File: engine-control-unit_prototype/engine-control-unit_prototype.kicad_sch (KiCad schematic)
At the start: 329 parts, among them IC1 TPS259573DSGR, J1 JTAG, J10 PORT_B, J11 PORT_C, J12 PORT_D, J13 PORT_A, J14 PORT_G, J15 PORT_F, J16 PORT_E, J17 2S_18650, J18 VALVE_IPA, J19 VALVE_NOS, J2 USB_C_Receptacle_USB2.0_man, J20 HEATER_IPA, J21 HEATER_NOS, J22 THERM2, J23 MAG_CONN_1, J24 MAG_CONN_2, J25 I2C_A, J26 THERM1, J27 I2C_B, J28 I2C_C, J29 I2C_D, J3 Micro_SD_Card_Det1, J4 PT1, J5 VREF, J6 PT1, J7 VREF, J8 FDCAN, J9 ADXL345, Q1 PMOS, Q2 NMOS, Q3 NPN, Q4 NMOS, Q5 NPN, Q6 NPN, SW1 BOOT, U1 USBLC6-2SC6, U10 TPS55285, U13 INA219AxD, U14 LT3042xMSE, U3 INA826, U4 INA826, U5 TCAN337G, U6 INA219AxD, U7 STM32H747II, U8 INA219AxD, U9 TPS55285, Y1 32.768KHz, Y2 25MHz

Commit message: Some fixes Back to subsheets Missing new ADC boost ldo for 3V3 now
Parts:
- removed C30: 0.1uF, Capacitor_SMD:C_0603_1608Metric_Pad1.08x0.95mm_HandSolder, symbol 0CSL_D1_V1:CAP_7mm_X_2mm
- removed C31: 10uF/50V, symbol Device:C_Polarized_US
- removed C32, C44, C53, C55, C57, C62, C63, C64, C65, C66, C75, C76, C77, C78, C79, C80, C81, C82, C83, C84, C85: C, symbol Device:C
- removed C33, C35, C40, C48, C49, C50, C52, C54, C56, C61, C86, C87, C88, C92: 0.1u, symbol Device:C
- removed C34, C41, C51: 10u, symbol Device:C
- removed C36, C37, C39, C42, C43, C45: ?, symbol Device:C
- removed C38: DNF, symbol Device:C
- removed C46: 100nF, symbol Device:C
- removed C47: 2.2u, symbol Device:C
- removed C58: CIN, symbol Device:C_Polarized_US
- removed C59: COUT, symbol Device:C_Polarized_US
- removed C60: CdV/dT, symbol Device:C
- removed C90, C91: 1uF, Capacitor_SMD:C_0603_1608Metric_Pad1.08x0.95mm_HandSolder, symbol Device:C
- removed D2: 6.4V, Diode_SMD:D_0603_1608Metric_Pad1.05x0.95mm_HandSolder, symbol 0CSL_D1_V1:DIODE_SCHOTTKY_30V_200mA
- removed D3: TVS SMBJ, symbol Device:D_Schottky
- removed D6: D_Zener, symbol Device:D_Zener
- removed F1: Polyfuse, Fuse:Fuse_0603_1608Metric_Pad1.05x0.95mm_HandSolder, symbol Device:Polyfuse_Small
- removed IC1: TPS259573DSGR, SON50P200X200X80-9N, symbol TPS259573DSGR:TPS259573DSGR
- removed J1: JTAG, UserFootprints:490107670612, symbol Connector_Generic:Conn_02x03_Counter_Clockwise
- removed J17: 2S_18650, symbol Connector:Screw_Terminal_01x02
- removed J2: USB_C_Receptacle_USB2.0_man, Connector_USB:USB_C_Receptacle_GCT_USB4105-xx-A_16P_TopMnt_Horizontal, symbol 0CSL_D1_V1:USB_C_Receptacle_USB2.0_man
- removed J22: THERM2, UserFootprints:MOLEX_5013310207, symbol Connector_Generic_MountingPin:Conn_01x02_MountingPin
- removed J25: I2C_A, symbol Connector:Conn_01x04_Socket
- removed J26: THERM1, UserFootprints:MOLEX_5013310207, symbol Connector_Generic_MountingPin:Conn_01x02_MountingPin
- removed J27: I2C_B, symbol Connector:Conn_01x04_Socket
- removed J28: I2C_C, symbol Connector:Conn_01x04_Socket
- removed J29: I2C_D, symbol Connector:Conn_01x04_Socket
- removed J3: Micro_SD_Card_Det1, UserFootprints:GCT_MEM2075-00-140-01-A, symbol Connector:Micro_SD_Card_Det1
- removed J4, J6: PT1, symbol Connector:Screw_Terminal_01x04
- removed J5, J7: VREF, symbol Connector:Conn_01x01_Pin
- removed J8: FDCAN, symbol Connector:DE9_Pins_MountingHoles
- removed J9: ADXL345, symbol Connector:Conn_01x09_Socket
- removed JP3, JP4: PIN/GND, symbol Jumper:Jumper_3_Bridged12
- removed L1, L2: L, symbol Device:L
- removed Q1: PMOS, symbol Simulation_SPICE:PMOS
- removed R1, R100, R101, R102, R11, R12, R140, R5, R7, R77, R78, R8, R9, R97, R98, R99: 0, symbol Device:R_US
- removed R10, R6, R67: ?, symbol Device:R_US
- removed R13, R22, R23, R25, R26, R27, R28, R30, R31, R37, R40, R55, R56, R57, R58, R59, R61, R63, R64, R70, R83, R84, R85, R86, R87, R88, R89, R90, R91, R92, R93, R94: R_US, symbol Device:R_US
- removed R14, R15, R16, R17, R18, R19, R20, R21, R24, R32, R33, R49, R50, R51, R52, R53, R54: 10k, symbol Device:R_US
- removed R29, R41: 10m, symbol Device:R_US
- removed R3, R4: 5.1k, symbol Device:R_US
- removed R60: 200k, symbol Device:R_US
- removed R62: DNF, symbol Device:R_US
- removed R68, R69: 10k, Resistor_SMD:R_0603_1608Metric_Pad0.98x0.95mm_HandSolder, symbol Device:R
- removed R81, R82: 60, symbol Device:R_US
- removed TP1: PT1, symbol Connector:TestPoint
- removed TP10: IN2-, symbol Connector:TestPoint
- removed TP11: IN3+, symbol Connector:TestPoint
- removed TP12: IN3-, symbol Connector:TestPoint
- removed TP13: VDD_3V3, symbol Connector:TestPoint
- removed TP14: CANH, symbol Connector:TestPoint
- removed TP15: CANL, symbol Connector:TestPoint
- removed TP16: TH1, symbol Connector:TestPoint
- removed TP17: TH2, symbol Connector:TestPoint
- removed TP2: PT2, symbol Connector:TestPoint
- removed TP3: VDD_10V, symbol Connector:TestPoint
- removed TP4: TPS10V_OUT, symbol Connector:TestPoint
- removed TP5: BATT1, symbol Connector:TestPoint
- removed TP6: VBATT_SAFE, symbol Connector:TestPoint
- removed TP7: IN1+, symbol Connector:TestPoint
- removed TP8: IN1-, symbol Connector:TestPoint
- removed TP9: IN2+, symbol Connector:TestPoint
- removed U1: USBLC6-2SC6, Package_TO_SOT_SMD:SOT-23-6, symbol Power_Protection:USBLC6-2SC6
- removed U10, U9: TPS55285, symbol SiriusLib:TPS55285
- removed U13, U6, U8: INA219AxD, Package_SO:SOIC-8_3.9x4.9mm_P1.27mm, symbol Sensor_Energy:INA219AxD
- removed U14: LT3042xMSE, Package_SO:MSOP-10-1EP_3x3mm_P0.5mm_EP1.68x1.88mm, symbol Regulator_Linear:LT3042xMSE
- removed U2: ~, Package_BGA:LFBGA-153_11.5x13mm_Layout14x14_P0.5mm, symbol FSU_LIB:ASFC32G31T3-51BIN
- removed U3, U4: INA826, UserFootprints:SOP65P490X110-8N, symbol INA826:INA826AIDGKR
- removed U5: TCAN337G, symbol Interface_CAN_LIN:TCAN337G
- added R144, R150, R153, R154: R_US, symbol Device:R_US
- added R151, R152, R157, R158, R159, R160, R161, R162, R163, R164, R165, R166, R167, R168, R169, R170, R171, R172, R173, R174, R175, R176, R177, R178, R179, R180, R181, R182, R183, R184, R185, R186, R187, R188, R189, R190, R191, R192, R193, R194, R195, R196, R197, R198, R199, R200, R201, R202, R203, R204, R205, R206, R207, R208, R209, R210, R211, R212, R213, R214, R215, R216, R217, R218, R219, R220, R221, R222, R223, R224, R225, R226, R227: 0, symbol Device:R_US
- R42: value 10m -> 0
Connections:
- net ADXL_CS is gone; now on an unnamed net: R114.2
- net ADXL_SCL is gone; now on an unnamed net: R111.2
- net ADXL_SDA is gone; now on an unnamed net: R112.2
- net D+ is gone; now on an unnamed net: R136.2
- net I2CD_SDA is gone; now on an unnamed net: R107.2
- net Psense2_IN+ is gone; now on net VDD_3V3: R42.1
- net SD_CLK is gone; now on an unnamed net: R79.2
- net SD_CMD is gone; now on an unnamed net: R80.2
- net SD_DAT0 is gone; now on an unnamed net: R95.2
- net SD_DAT1 is gone; now on an unnamed net: R96.2
- net THERM1 is gone; now on an unnamed net: R109.2
- net TPS10V_SCL is gone; now on an unnamed net: R106.2
- net TPS3V3_SCL is gone; now on an unnamed net: R104.2
- net DATA_S1: no longer R122.2
- net DATA_S2: no longer R123.2
- net GND: now also R150.1, R153.1, R154.1; no longer Q3.3 (E), Q5.3 (E), Q6.3 (E)
- net LSE0: no longer R129.2
- net LSE1: no longer R130.2
- net NRST: now also R144.2; no longer R125.2
- net VDD_3V3: no longer R42.2
- net VDD_MCU: now also R144.1
- net at J15.1 (Pin_1): now also R115.1; no longer U7.18 (PF0)
- net at J15.10 (Pin_10): now also R124.1; no longer U7.29 (PF9)
- net at J15.11 (Pin_11): now also R125.1; no longer U7.30 (PF10)
- net at J15.12 (Pin_12): now also R126.1; no longer U7.58 (PF11)
- net at J15.13 (Pin_13): now also R127.1; no longer U7.59 (PF12)
- net at J15.14 (Pin_14): now also R128.1; no longer U7.60 (PF13)
- net at J15.15 (Pin_15): now also R129.1; no longer U7.61 (PF14)
- net at J15.16 (Pin_16): now also R130.1; no longer U7.62 (PF15)
- net at J15.2 (Pin_2): now also R116.1; no longer U7.19 (PF1)
- net at J15.3 (Pin_3): now also R117.1; no longer U7.20 (PF2)
- net at J15.4 (Pin_4): now also R118.1; no longer U7.21 (PF3)
- net at J15.5 (Pin_5): now also R119.1; no longer U7.22 (PF4)
- net at J15.6 (Pin_6): now also R120.1; no longer U7.23 (PF5)
- net at J15.7 (Pin_7): now also R121.1; no longer U7.26 (PF6)
- net at J15.8 (Pin_8): now also R122.1; no longer U7.27 (PF7)
- net at J15.9 (Pin_9): now also R123.1; no longer U7.28 (PF8)
- net at R136.1: now also J10.3 (Pin_3)
- net at J16.1 (Pin_1): now also R196.2; no longer U7.170 (PE0)
- net at J16.10 (Pin_10): now also R205.2; no longer U7.69 (PE9)
- net at J16.11 (Pin_11): now also R206.2; no longer U7.72 (PE10)
- net at J16.12 (Pin_12): now also R207.2; no longer U7.73 (PE11)
- net at U7.74 (PE12): now also R208.1; no longer J16.13 (Pin_13)
- net at J16.14 (Pin_14): now also R209.2; no longer U7.75 (PE13)
- net at J16.15 (Pin_15): now also R210.2; no longer U7.76 (PE14)
- net at J16.16 (Pin_16): now also R211.2; no longer U7.77 (PE15)
- net at J16.2 (Pin_2): now also R197.2; no longer U7.171 (PE1)
- net at J16.3 (Pin_3): now also R198.2; no longer U7.1 (PE2)
- net at J16.4 (Pin_4): now also R199.2; no longer U7.2 (PE3)
- net at J16.5 (Pin_5): now also R200.2; no longer U7.3 (PE4)
- net at U7.4 (PE5): now also R201.1; no longer J16.6 (Pin_6)
- net at J16.7 (Pin_7): now also R202.2; no longer U7.5 (PE6)
- net at J16.8 (Pin_8): now also R203.2; no longer U7.67 (PE7)
- net at J16.9 (Pin_9): now also R204.2; no longer U7.68 (PE8)
- net at R107.1: now also J14.9 (Pin_9)
- net at R95.1: now also J14.3 (Pin_3)
- net at J10.1 (Pin_1): now also R133.1; no longer U7.55 (PB0)
- net at J10.10 (Pin_10): now also R157.1; no longer U7.169 (PB9)
- net at J10.11 (Pin_11): now also R158.1; no longer U7.78 (PB10)
- net at J10.12 (Pin_12): now also R159.1; no longer U7.79 (PB11)
- net at J10.13 (Pin_13): now also R160.1; no longer U7.85 (PB12)
- net at J10.14 (Pin_14): now also R161.1; no longer U7.86 (PB13)
- net at J10.15 (Pin_15): now also R162.1; no longer U7.87 (PB14)
- net at J10.16 (Pin_16): now also R163.1; no longer U7.88 (PB15)
- net at J10.2 (Pin_2): now also R134.1; no longer U7.56 (PB1)
- net at U7.57 (PB2): no longer J10.3 (Pin_3)
- net at J10.4 (Pin_4): now also R137.1; no longer U7.162 (PB3)
- net at J10.5 (Pin_5): now also R141.1; no longer U7.163 (PB4)
- net at J10.6 (Pin_6): now also R142.1; no longer U7.164 (PB5)
- net at J10.7 (Pin_7): now also R143.1; no longer U7.165 (PB6)
- net at J10.8 (Pin_8): now also R151.1; no longer U7.166 (PB7)
- net at J10.9 (Pin_9): now also R152.1; no longer U7.168 (PB8)
- net at J13.1 (Pin_1): now also R212.2; no longer U7.41 (PA0)
- net at J13.10 (Pin_10): now also R221.2; no longer U7.128 (PA9)
- net at J13.11 (Pin_11): now also R222.2; no longer U7.129 (PA10)
- net at U7.130 (PA11): now also R223.1; no longer J13.12 (Pin_12)
- net at J13.13 (Pin_13): now also R224.2; no longer U7.131 (PA12)
- net at J13.14 (Pin_14): now also R225.2; no longer U7.132 (PA13)
- net at U7.138 (PA14): now also R226.1; no longer J13.15 (Pin_15)
- net at J13.16 (Pin_16): now also R227.2; no longer U7.139 (PA15)
- net at U7.42 (PA1): now also R213.1; no longer J13.2 (Pin_2)
- net at J13.3 (Pin_3): now also R214.2; no longer U7.43 (PA2)
- net at J13.4 (Pin_4): now also R215.2; no longer U7.46 (PA3)
- net at J13.5 (Pin_5): now also R216.2; no longer U7.49 (PA4)
- net at J13.6 (Pin_6): now also R217.2; no longer U7.50 (PA5)
- net at J13.7 (Pin_7): now also R218.2; no longer U7.51 (PA6)
- net at J13.8 (Pin_8): now also R219.2; no longer U7.52 (PA7)
- net at J13.9 (Pin_9): now also R220.2; no longer U7.127 (PA8)
- net at U7.143 (PD0): now also R180.1; no longer J12.1 (Pin_1)
- net at J12.10 (Pin_10): now also R189.2; no longer U7.90 (PD9)
- net at J12.11 (Pin_11): now also R190.2; no longer U7.91 (PD10)
- net at J12.12 (Pin_12): now also R191.2; no longer U7.94 (PD11)
- net at U7.95 (PD12): now also R192.1; no longer J12.13 (Pin_13)
- net at J12.14 (Pin_14): now also R193.2; no longer U7.96 (PD13)
- net at J12.15 (Pin_15): now also R194.2; no longer U7.97 (PD14)
- net at J12.16 (Pin_16): now also R195.2; no longer U7.98 (PD15)
- net at J12.2 (Pin_2): now also R181.2; no longer U7.144 (PD1)
- net at J12.3 (Pin_3): now also R182.2; no longer U7.145 (PD2)
- net at J12.4 (Pin_4): now also R183.2; no longer U7.146 (PD3)
- net at J12.5 (Pin_5): now also R184.2; no longer U7.147 (PD4)
- net at J12.6 (Pin_6): now also R185.2; no longer U7.148 (PD5)
- net at J12.7 (Pin_7): now also R186.2; no longer U7.149 (PD6)
- net at U7.150 (PD7): now also R187.1; no longer J12.8 (Pin_8)
- net at J12.9 (Pin_9): now also R188.2; no longer U7.89 (PD8)
- net at R104.1: now also J14.6 (Pin_6)
- net at R96.1: now also J14.4 (Pin_4)
- net at U7.10 (PC14): now also R178.2; no longer J11.15 (Pin_15)
- net at U7.11 (PC15): now also R179.2; no longer J11.16 (Pin_16)
- net at J11.7 (Pin_7): now also R170.1; no longer U7.122 (PC6)
- net at J11.8 (Pin_8): now also R171.1; no longer U7.123 (PC7)
- net at U7.124 (PC8): now also R172.2; no longer J11.9 (Pin_9)
- net at J11.10 (Pin_10): now also R173.1; no longer U7.125 (PC9)
- net at J11.11 (Pin_11): now also R174.1; no longer U7.140 (PC10)
- net at U7.141 (PC11): now also R175.2; no longer J11.12 (Pin_12)
- net at J11.13 (Pin_13): now also R176.1; no longer U7.142 (PC12)
- net at U7.34 (PC0): now also R164.2; no longer J11.1 (Pin_1)
- net at U7.35 (PC1): now also R165.2; no longer J11.2 (Pin_2)
- net at U7.36 (PC2_C): now also R166.2; no longer J11.3 (Pin_3)
- net at U7.37 (PC3_C): now also R167.2; no longer J11.4 (Pin_4)
- net at U7.53 (PC4): now also R168.2; no longer J11.5 (Pin_5)
- net at J11.6 (Pin_6): now also R169.1; no longer U7.54 (PC5)
- net at J11.14 (Pin_14): now also R177.1; no longer U7.9 (PC13)
- net at R114.1: now also J14.16 (Pin_16)
- net at R79.1: now also J14.1 (Pin_1)
- net at R106.1: now also J14.8 (Pin_8)
- net at U7.110 (PG2): no longer J14.3 (Pin_3)
- net at U7.111 (PG3): no longer J14.4 (Pin_4)
- net at J14.5 (Pin_5): now also R103.1; no longer U7.114 (PG4)
- net at U7.115 (PG5): no longer J14.6 (Pin_6)
- net at J14.7 (Pin_7): now also R105.1; no longer U7.116 (PG6)
- net at U7.117 (PG7): no longer J14.8 (Pin_8)
- net at U7.118 (PG8): no longer J14.9 (Pin_9)
- net at J14.10 (Pin_10): now also R108.1; no longer U7.153 (PG9)
- net at U7.154 (PG10): no longer J14.11 (Pin_11)
- net at J14.12 (Pin_12): now also R110.1; no longer U7.155 (PG11)
- net at U7.156 (PG12): no longer J14.13 (Pin_13)
- net at U7.157 (PG13): no longer J14.14 (Pin_14)
- net at J14.15 (Pin_15): now also R113.1; no longer U7.158 (PG14)
- net at U7.161 (PG15): no longer J14.16 (Pin_16)
- net at U7.63 (PG0): no longer J14.1 (Pin_1)
- net at U7.66 (PG1): no longer J14.2 (Pin_2)
- net at R80.1: now also J14.2 (Pin_2)
- net at R111.1: now also J14.13 (Pin_13)
- net at R112.1: now also J14.14 (Pin_14)
- net at R109.1: now also J14.11 (Pin_11)
- net ADXL_SDO: no longer names the net of R113.2
- net ADXL_SDO: now also U7.158 (PG14)
- net BUZ: no longer names the net of R124.2
- net BUZ: now also U7.29 (PF9)
- net D-: no longer names the net of R137.2
- net D-: now also U7.162 (PB3)
- net EFUSE_FLT: no longer names the net of R141.2
- net EFUSE_FLT: now also U7.163 (PB4)
- net I2CD_SCL: no longer names the net of R108.2
- net I2CD_SCL: now also U7.153 (PG9)
- net PT1: no longer names the net of R133.2
- net PT1: now also U7.55 (PB0)
- net PT2: no longer names the net of R134.2
- net PT2: now also U7.56 (PB1)
- net SD_DAT2: no longer names the net of R115.2
- net SD_DAT2: now also U7.18 (PF0)
- net SD_DAT3: no longer names the net of R116.2
- net SD_DAT3: now also U7.19 (PF1)
- net SD_DET: no longer names the net of R117.2
- net SD_DET: now also U7.20 (PF2)
- net SWCLK: no longer names the net of R127.2
- net SWCLK: now also U7.59 (PF12)
- net SWDIO: no longer names the net of R126.2
- net SWDIO: now also U7.58 (PF11)
- net SWO: no longer names the net of R128.2
- net SWO: now also U7.60 (PF13)
- net TCAN_FLT: no longer names the net of R120.2
- net TCAN_FLT: now also U7.23 (PF5)
- net TCAN_RX: no longer names the net of R118.2
- net TCAN_RX: now also U7.21 (PF3)
- net TCAN_STBY: no longer names the net of R121.2
- net TCAN_STBY: now also U7.26 (PF6)
- net TCAN_TX: no longer names the net of R119.2
- net TCAN_TX: now also U7.22 (PF4)
- net THERM2: no longer names the net of R110.2
- net THERM2: now also U7.155 (PG11)
- net TPS10V_INT: no longer names the net of R142.2
- net TPS10V_INT: now also U7.164 (PB5)
- net TPS10V_SDA: no longer names the net of R105.2
- net TPS10V_SDA: now also U7.116 (PG6)
- net TPS3V3_INT: no longer names the net of R143.2
- net TPS3V3_INT: now also U7.165 (PB6)
- net TPS3V3_SDA: no longer names the net of R103.2
- net TPS3V3_SDA: now also U7.114 (PG4)
- net VDDA renamed VDDA_MCU
- net VDDA_MCU: now also R42.2
- new net: J16.13 (Pin_13), R208.2
- new net: R177.2, U7.9 (PC13)
- new net: J16.6 (Pin_6), R201.2
- new net: R171.2, U7.123 (PC7)
- new net: J13.15 (Pin_15), R226.2
- new net: R176.2, U7.142 (PC12)
- new net: Q5.3 (E), R153.2
- new net: J13.12 (Pin_12), R223.2
- new net: R122.2, U7.27 (PF7)
- new net: J13.2 (Pin_2), R213.2
- new net: Q6.3 (E), R150.2
- new net: R158.2, U7.78 (PB10)
- new net: J12.13 (Pin_13), R192.2
- new net: R125.2, U7.30 (PF10)
- new net: R173.2, U7.125 (PC9)
- new net: R216.1, U7.49 (PA4)
- new net: J12.1 (Pin_1), R180.2
- new net: R217.1, U7.50 (PA5)
- new net: R159.2, U7.79 (PB11)
- new net: J12.8 (Pin_8), R187.2
- new net: Q3.3 (E), R154.2
- new net: R162.2, U7.87 (PB14)
- new net: R174.2, U7.140 (PC10)
- new net: R207.1, U7.73 (PE11)
- new net: R169.2, U7.54 (PC5)
- new net: R202.1, U7.5 (PE6)
- new net: R170.2, U7.122 (PC6)
- new net: R186.1, U7.149 (PD6)
- new net: R189.1, U7.90 (PD9)
- new net: R218.1, U7.51 (PA6)
- new net: R161.2, U7.86 (PB13)
- new net: R181.1, U7.144 (PD1)
- new net: R185.1, U7.148 (PD5)
- new net: R194.1, U7.97 (PD14)
- new net: R209.1, U7.75 (PE13)
- new net: R204.1, U7.68 (PE8)
- new net: R129.2, U7.61 (PF14)
- new net: R182.1, U7.145 (PD2)
- new net: R183.1, U7.146 (PD3)
- new net: R184.1, U7.147 (PD4)
- new net: R151.2, U7.166 (PB7)
- new net: R152.2, U7.168 (PB8)
- new net: R157.2, U7.169 (PB9)
- new net: R160.2, U7.85 (PB12)
- new net: R163.2, U7.88 (PB15)
- new net: R188.1, U7.89 (PD8)
- new net: R190.1, U7.91 (PD10)
- new net: R191.1, U7.94 (PD11)
- new net: R193.1, U7.96 (PD13)
- new net: R195.1, U7.98 (PD15)
- new net: R224.1, U7.131 (PA12)
- new net: R206.1, U7.72 (PE10)
- new net: R220.1, U7.127 (PA8)
- new net: R203.1, U7.67 (PE7)
- new net: J11.16 (Pin_16), R179.1
- new net: R214.1, U7.43 (PA2)
- new net: R212.1, U7.41 (PA0)
- new net: J11.9 (Pin_9), R172.1
- new net: R227.1, U7.139 (PA15)
- new net: R219.1, U7.52 (PA7)
- new net: R198.1, U7.1 (PE2)
- new net: R221.1, U7.128 (PA9)
- new net: R222.1, U7.129 (PA10)
- new net: R225.1, U7.132 (PA13)
- new net: R196.1, U7.170 (PE0)
- new net: R197.1, U7.171 (PE1)
- new net: R199.1, U7.2 (PE3)
- new net: R123.2, U7.28 (PF8)
- new net: R200.1, U7.3 (PE4)
- new net: R215.1, U7.46 (PA3)
- new net: R130.2, U7.62 (PF15)
- new net: R205.1, U7.69 (PE9)
- new net: R210.1, U7.76 (PE14)
- new net: R211.1, U7.77 (PE15)
- new net: J11.2 (Pin_2), R165.1
- new net: J11.15 (Pin_15), R178.1
- new net: J11.4 (Pin_4), R167.1
- new net: J11.3 (Pin_3), R166.1
- new net: J11.1 (Pin_1), R164.1
- new net: J11.12 (Pin_12), R175.1
- new net: J11.5 (Pin_5), R168.1
- no-connect marks 21 -> 11
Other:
- added sheet ADC (adc.kicad_sch)
- added sheet COMMUNICATION (communication.kicad_sch)
- added sheet POWER (power.kicad_sch)
- added sheet STORAGE (storage.kicad_sch)
- note removed: "(1) This resistor is optional if the input voltage stays above [(V-) - 2 V] or if the signal source current drive capability is limited to less than 3.5 mA; see the Input Protection section for more details."
- note removed: "(2) The output of the INA826 is referred to the output reference (REF) terminal, which is normally grounded. This connection must be low-impedance to maintain good common-mode rejection. Although 5 Ω or less of stray resistance can be tolerated when maintaining specified CMRR, small stray resistances of tens of ohms in series with the REF pin can cause noticeable degradation in CMRR."
- note removed: "(3) Pour filtrage si nécéssaire"
- note removed: "(4) Proche des pins d'alim"
- note removed: "(5) Gain = 1 + $9.4k/Rg"
- note removed: "10V REGULATION"
- note removed: "3V3 REGULATION"
- note removed: "ASFC32G31T3-51BIN"
- note removed: "C0G ?"
- note removed: "Calcul des compos"
- note removed: "Changer connecteurs pour connecteur 5 pin à Greg"
- note removed: "Dont forget to add magnetic encoder"
- note removed: "FDCAN"
- note removed: "INPUT PROTECTION"
- note removed: "Impédance match data = 50±5 ohm"
- note removed: "Jumper pour adresses ?"
- note removed: "Loop du vdd ou non ?"
- note removed: "PINS TO MAP"
- note removed: "PORTS"
- note removed: "POWER/CURRENT MONITOR"
- note removed: "PRESSURE TRANSDUCERS"
- note removed: "Power ? Ou 10V enough ?"
- note removed: "Reference design : https://media.digikey.com/pdf/Data%20Sheets/Octavo%20PDFs/DesigningForFlexibilityAround-EMMC.pdf page 7"
- note removed: "SD CARD"
- note removed: "THERMISTORS"
- note removed: "TPS55285"
- note removed: "USB-C/PROG"
- note removed: "eMMC"
- moved on the sheet: BZ1, D4, D5, J10, J11, J12, J13, J14, J15, J16, J18, J19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

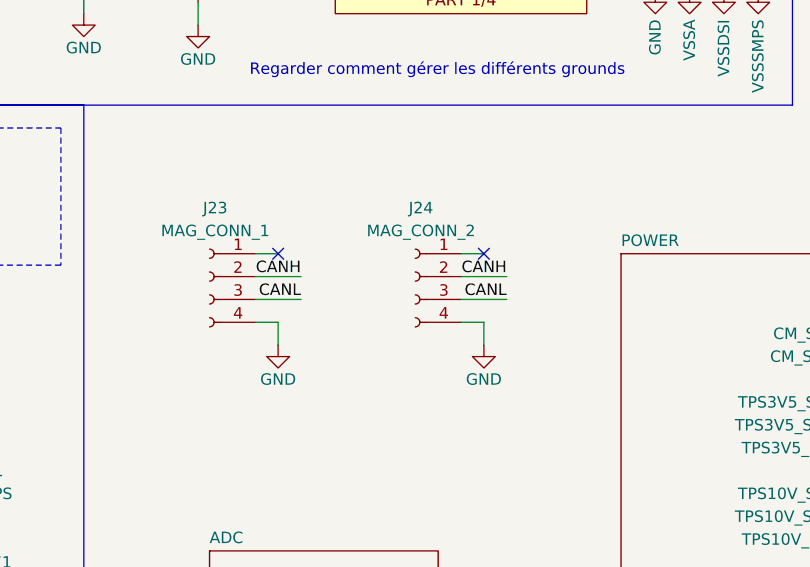
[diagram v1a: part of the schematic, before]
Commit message: Added subsheets
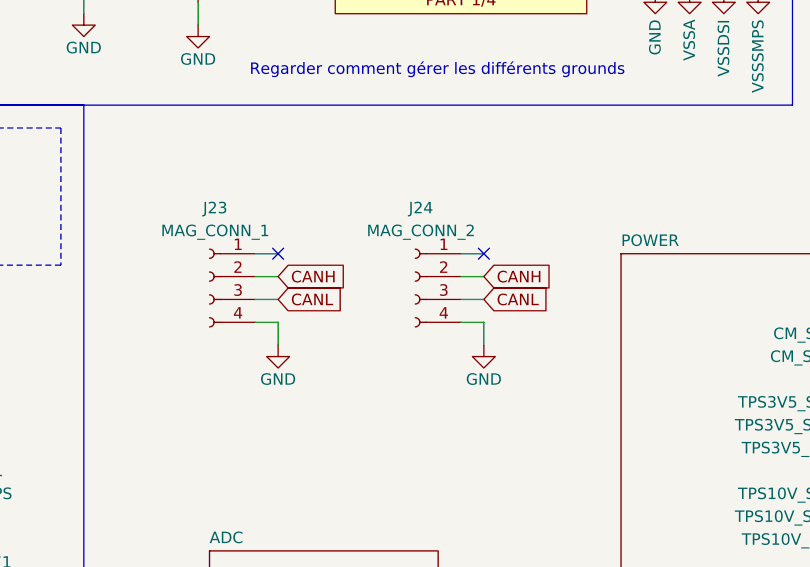
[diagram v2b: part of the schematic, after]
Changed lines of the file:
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@@
 	(wire
 		(pts
-			(xy 199.39 158.75) (xy 194.31 158.75)
+			(xy 196.85 158.75) (xy 194.31 158.75)
 		)
 		(stroke
@@
 	(wire
 		(pts
-			(xy 222.25 158.75) (xy 217.17 158.75)
+			(xy 219.71 158.75) (xy 217.17 158.75)
 		)
 		(stroke
@@
 	(wire
 		(pts
-			(xy 222.25 161.29) (xy 217.17 161.29)
+			(xy 219.71 161.29) (xy 217.17 161.29)
 		)
 		(stroke
@@
 	(wire
 		(pts
-			(xy 199.39 161.29) (xy 194.31 161.29)
+			(xy 196.85 161.29) (xy 194.31 161.29)
 		)
 		(stroke
@@
 		)
 	)
-	(label "CANL"
-		(at 199.39 161.29 180)
-		(effects
-			(font
-				(size 1.27 1.27)
-			)
-			(justify right bottom)
-		)
-	)
 	(label "eMMC_DAT1"
 		(at 405.13 231.14 180)
@@
 		)
 	)
-	(label "CANH"
-		(at 199.39 158.75 180)
-		(effects
-			(font
-				(size 1.27 1.27)
-			)
-			(justify right bottom)
-		)
-	)
-	(label "CANL"
-		(at 222.25 161.29 180)
-		(effects
-			(font
-				(size 1.27 1.27)
-			)
-			(justify right bottom)
-		)
-	)
 	(label "NRST"
 		(at 57.15 86.36 0)
@@
 		)
 	)
-	(label "CANH"
-		(at 222.25 158.75 180)
-		(effects
-			(font
-				(size 1.27 1.27)
-			)
-			(justify right bottom)
-		)
-	)
 	(label "LSE1"
 		(at 48.26 27.94 180)
@@
 		)
 	)
+	(global_label "CANL"
+		(shape input)
+		(at 219.71 161.29 0)
+		(fields_autoplaced yes)
+		(effects
+			(font
+				(size 1.27 1.27)
+			)
+			(justify left)
+		)
+		(property "Intersheetrefs" "${INTERSHEET_REFS}"
+			(at 227.4124 161.29 0)
+			(effects
+				(font
+					(size 1.27 1.27)
+				)
+				(justify left)
+				(hide yes)
+			)
+		)
+	)
+	(global_label "CANH"
+		(shape input)
+		(at 219.71 158.75 0)
+		(fields_autoplaced yes)
+		(effects
+			(font
+				(size 1.27 1.27)
+			)
+			(justify left)
+		)
+		(property "Intersheetrefs" "${INTERSHEET_REFS}"
+			(at 227.7148 158.75 0)
+			(effects
+				(font
+					(size 1.27 1.27)
+				)
+				(justify left)
+				(hide yes)
+			)
+		)
+	)
+	(global_label "CANL"
+		(shape input)
+		(at 196.85 161.29 0)
+		(fields_autoplaced yes)
+		(effects
+			(font
+				(size 1.27 1.27)
+			)
+			(justify left)
+		)
+		(property "Intersheetrefs" "${INTERSHEET_REFS}"
+			(at 204.5524 161.29 0)
+			(effects
+				(font
+					(size 1.27 1.27)
+				)
+				(justify left)
+				(hide yes)
+			)
+		)
+	)
+	(global_label "CANH"
+		(shape input)
+		(at 196.85 158.75 0)
+		(fields_autoplaced yes)
+		(effects
+			(font
+				(size 1.27 1.27)
+			)
+			(justify left)
+		)
+		(property "Intersheetrefs" "${INTERSHEET_REFS}"
+			(at 204.8548 158.75 0)
+			(effects
+				(font
+					(size 1.27 1.27)
+				)
+				(justify left)
+				(hide yes)
+			)
+		)
+	)

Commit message: Added Control page Revisited power tree (VDDA_3V3 and VDD_3V3) Bunch of other fixes
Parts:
- removed BZ1: Buzzer_TDK_PS1240, 0CSL_D1_V1:Buzzer_TDK_PS1240P02BT_D12.2mmP5mm, symbol 0CSL_D1_V1:Buzzer_TDK_PS1240
- removed C67: 4.7u ESR < 100m, symbol Device:C
- removed C68, C69: 2.2u ESR < 100m, symbol Device:C
- removed C70, C71: 4.7u, symbol Device:C
- removed C72: 220p, symbol Device:C
- removed C73, C74: 10u ESR < 20m, symbol Device:C
- removed D4, D5: BAV99, Package_TO_SOT_SMD:SOT-23, symbol Diode:BAV99
- removed J18: VALVE_IPA, symbol Connector:Screw_Terminal_01x03
- removed J19: VALVE_NOS, symbol Connector:Screw_Terminal_01x03
- removed J20: HEATER_IPA, symbol Connector:Screw_Terminal_01x02
- removed J21: HEATER_NOS, symbol Connector:Screw_Terminal_01x02
- removed J23: MAG_CONN_1, symbol Connector:Conn_01x04_Socket
- removed J24: MAG_CONN_2, symbol Connector:Conn_01x04_Socket
- removed JP1: LSE_OSC, symbol Jumper:SolderJumper_2_Open
- removed JP10, JP11, JP12, JP6, JP7: SMPS, symbol Jumper:SolderJumper_2_Open
- removed JP2: HSE_OSC, symbol Jumper:SolderJumper_2_Open
- removed JP5, JP8, JP9: LDO, symbol Jumper:SolderJumper_2_Open
- removed L3: FBMJ1608HM180NTR, symbol Device:L_Ferrite
- removed L4: 2.2u, symbol Device:L
- removed Q2, Q4: NMOS, symbol Simulation_SPICE:NMOS
- removed Q3, Q5, Q6: NPN, symbol Simulation_SPICE:NPN
- removed R135, R138: 0, symbol Device:R_US
- removed R150, R153, R154, R71, R72, R73, R74, R75, R76: R_US, symbol Device:R_US
- removed R65, R66: 10k, Resistor_SMD:R_0603_1608Metric_Pad0.98x0.95mm_HandSolder, symbol 0CSL_D1_V1:RES0603
- removed TP18: S1, symbol Connector:TestPoint
- removed TP19: S2, symbol Connector:TestPoint
- added R230, R231: 0, Resistor_SMD:R_0201_0603Metric, symbol Device:R_US
- C1, C10, C11, C12, C13, C14, C15, C16, C17, C18, C19, C2, C20, C23, C25, C26, C28, C29, C3, C4, C5, C6, C7, C8, C9: footprint (none) -> Capacitor_SMD:C_0603_1608Metric
- R103, R104, R105, R106, R107, R108, R109, R110, R111, R112, R113, R114, R115, R116, R117, R118, R119, R120, R121, R122, R123, R124, R125, R126, R127, R128, R129, R130, R131, R132, R133, R134, R136, R137, R139, R141, R142, R143, R151, R152, R157, R158, R159, R160, R161, R162, R163, R164, R165, R166, R167, R168, R169, R170, R171, R172, R173, R174, R175, R176, R177, R178, R179, R180, R181, R182, R183, R184, R185, R186, R187, R188, R189, R190, R191, R192, R193, R194, R195, R196, R197, R198, R199, R2, R200, R201, R202, R203, R204, R205, R206, R207, R208, R209, R210, R211, R212, R213, R214, R215, R216, R217, R218, R219, R220, R221, R222, R223, R224, R225, R226, R227, R34, R35, R36, R38, R39, R42, R43, R44, R45, R46, R47, R48, R79, R80, R95, R96: footprint (none) -> Resistor_SMD:R_0201_0603Metric
- R144: footprint (none) -> Resistor_SMD:R_0402_1005Metric
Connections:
- net GNDA is gone; now on net GND: C24.2, C25.2
- net HSE1: now also Y2.3
- net LSE0: now also R231.1; no longer Y1.1
- net LSE1: now also R230.2
- net at Y1.3: now also R230.1
- new net: R231.2, Y1.1
- no-connect marks 11 -> 7
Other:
- added sheet CONTROL (control.kicad_sch)
- sheet ADC ports: added ADS_CLKIN, ADS_CS, ADS_DIN, ADS_DOUT, ADS_DRDY, ADS_SCLK, ADS_SYNC/RESET; removed PT2
- sheet POWER ports: added PM_SCL, PM_SDA; removed CM_SCL, CM_SDA
- note added: "Découplage ?"
- note added: "GND tous gnd"
- note added: "Max freq emmc pour ringing ?"
- note added: "Mettre power flags dans power et test points"
- note added: "Mettre values"
- note removed: "(1)"
- note removed: "(1) Jumpers pour choix entre SMPS direct ou SMPS externe avec LDO par SMPS"
- note removed: "(2)"
- note removed: "(2) Bead utilisé dans eval board"
- note removed: "(3)"
- note removed: "(3) Choix des condensateurs pour SMPS [p.103, p.110 | stm32h757ai.pdf]"
- note removed: "(4)"
- note removed: "(4) Datasheet dit 4.7uF, mais eval board met 10uF"
- note removed: "Datasheet STM32H747"
- note removed: "Placer proche L1"
- note removed: "Regarder comment gérer les différents grounds"
- note removed: "SMPS"
- note removed: "Schematic Eval board STM32H7X7"
- moved on the sheet: Y1

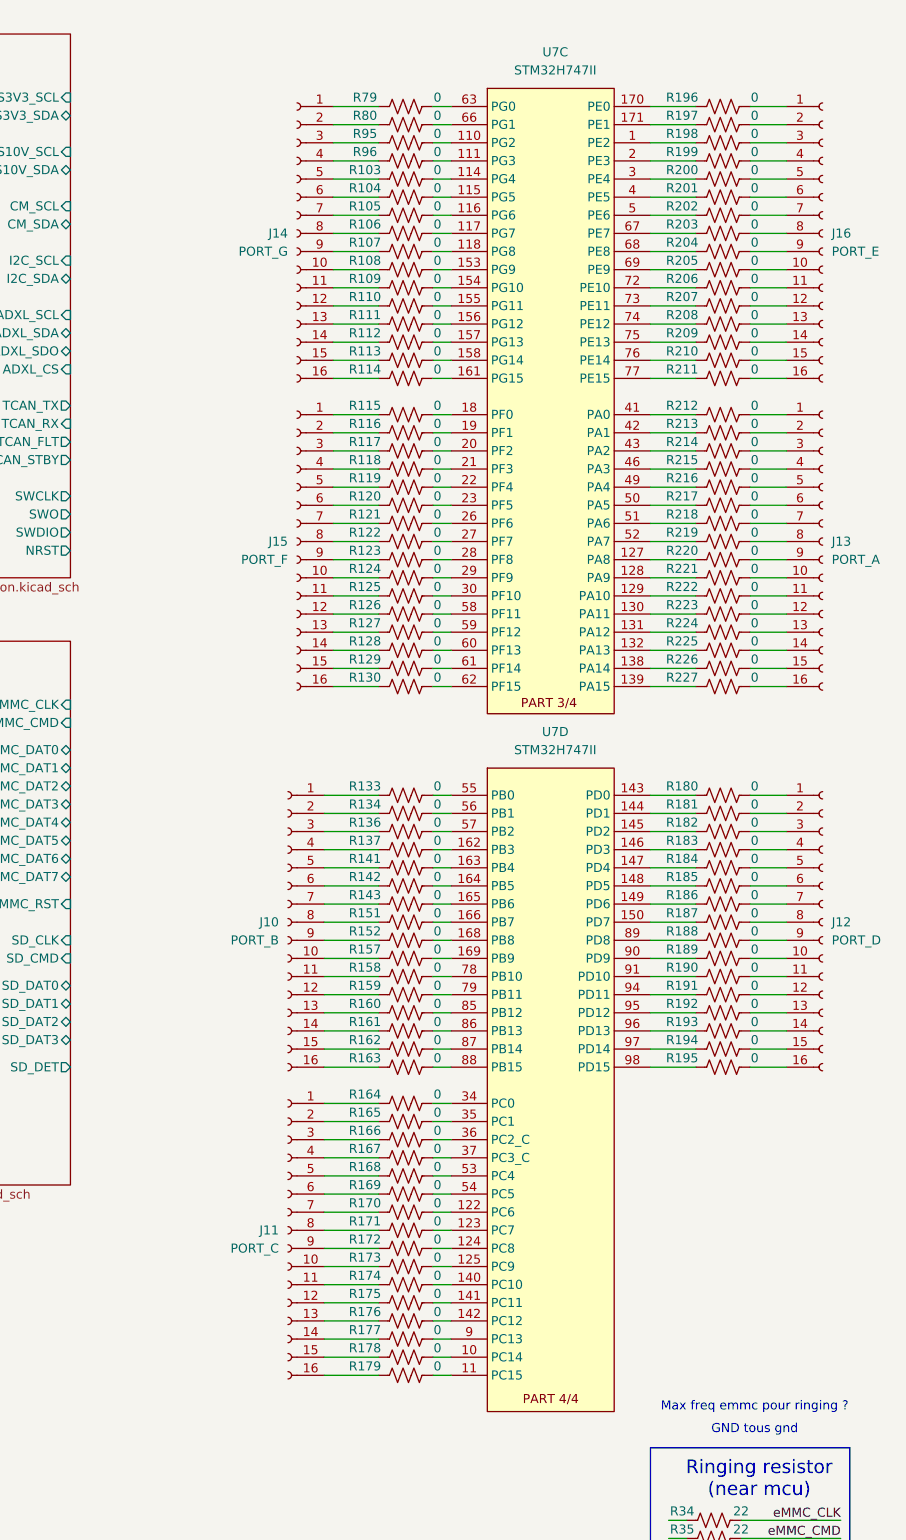
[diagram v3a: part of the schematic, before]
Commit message: Fixed inverted LED diodes (oops) Replaced 3x INA219 with INA3221
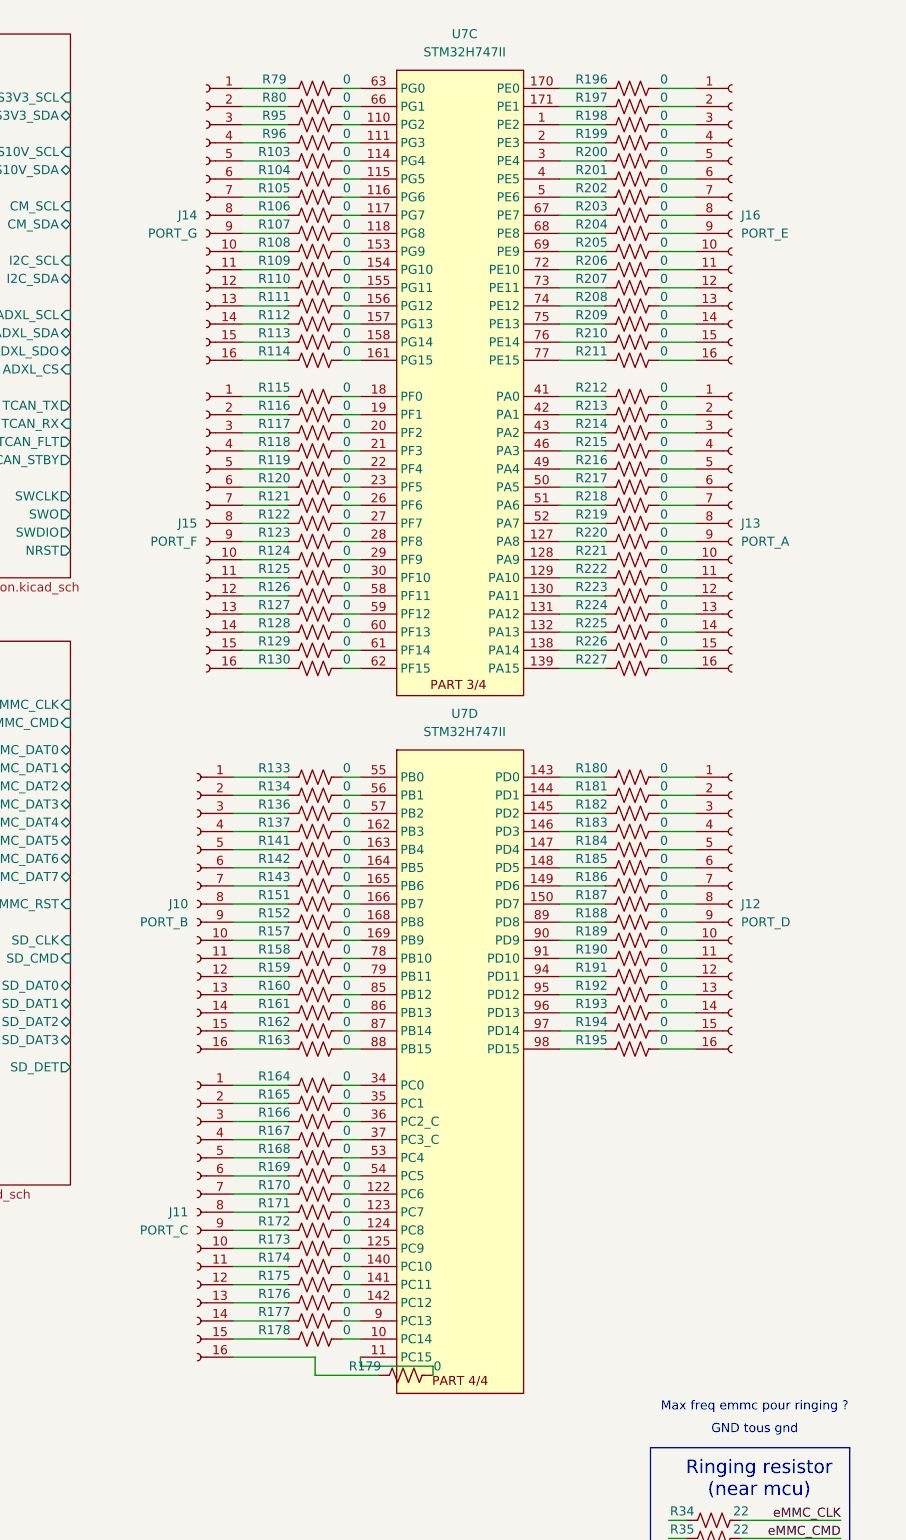
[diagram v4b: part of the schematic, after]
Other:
- moved on the sheet: J10, J11, J12, J13, J14, J15, J16, R103, R104, R105, R106, R107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

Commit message: Added magnetic encoders Added optional external valve control connector
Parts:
- added C88, C89: 2u2, Capacitor_SMD:C_0603_1608Metric, symbol Device:C
- renumbered C24 to C22, C25 to C23, C22 to C24, C23 to C25, J14 to J1, J16 to J2, J15 to J3, J13 to J4, J10 to J5, J12 to J6, J11 to J7, R2 to R1, R96 to R10, R193 to R100, R162 to R101, R194 to R102, R163 to R103, R195 to R104, R164 to R105, R165 to R106, R166 to R107, R167 to R108, R168 to R109, R199 to R11, R169 to R110, R170 to R111, R171 to R112, R172 to R113, R173 to R114, R174 to R115, R175 to R116, R176 to R117, R177 to R118, R178 to R119, R103 to R12, R179 to R120, R34 to R121, R35 to R122, R36 to R123, R38 to R124, R39 to R125, R43 to R126, R44 to R127, R45 to R128, R46 to R129, R200 to R13, R47 to R130, R48 to R131, R139 to R14, R42 to R15, R104 to R16, R201 to R17, R105 to R18, R202 to R19, R79 to R2, R106 to R20, R203 to R21, R107 to R22, R204 to R23, R108 to R24, R205 to R25, R109 to R26, R206 to R27, R110 to R28, R207 to R29, R196 to R3, R111 to R30, R208 to R31, R112 to R32, R209 to R33, R113 to R34, R210 to R35, R114 to R36, R211 to R37, R115 to R38, R212 to R39, R80 to R4, R116 to R40, R213 to R41, R117 to R42, R214 to R43, R118 to R44, R215 to R45, R119 to R46, R216 to R47, R120 to R48, R217 to R49, R197 to R5, R144 to R50, R121 to R51, R218 to R52, R122 to R53, R219 to R54, R131 to R55, R123 to R56, R220 to R57, R132 to R58, R124 to R59, R231 to R6, R221 to R60, R125 to R61, R222 to R62, R126 to R63, R223 to R64, R127 to R65, R224 to R66, R128 to R67, R225 to R68, R129 to R69, R230 to R7, R226 to R70, R130 to R71, R227 to R72, R133 to R73, R180 to R74, R134 to R75, R181 to R76, R136 to R77, R182 to R78, R137 to R79, R95 to R8, R183 to R80, R141 to R81, R184 to R82, R142 to R83, R185 to R84, R143 to R85, R186 to R86, R151 to R87, R187 to R88, R152 to R89, R198 to R9, R188 to R90, R157 to R91, R189 to R92, R158 to R93, R190 to R94, R159 to R95, R191 to R96, R160 to R97, R192 to R98, R161 to R99, U7 to U1
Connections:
- net GND: now also C88.2, C89.2
- net VCAP: now also C88.1, C89.1
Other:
- sheet CONTROL ports: added BUZZ, IPA_DATA, IPA_ENC-M1, IPA_ENC-M2, IPA_ENC-OUTA, IPA_ENC-OUTB, IPA_HEAT, NOS_DATA, NOS_ENC-M1, NOS_ENC-M2, NOS_ENC-OUTA, NOS_ENC-OUTB, NOS_HEAT; removed none
- sheet POWER ports: added PM_CRIT, PM_TC, PM_WARN; removed none
- note added: "Next V, jumper for gnda"
- moved on the sheet: C26, C27, R120

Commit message: VDD_3V3 is now VDD_3V6 (Removed LDO) LEDs now have the right symbol (oops x2)
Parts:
- removed R121, R122, R123, R124, R125, R126, R127, R128, R129, R130, R131: 22, Resistor_SMD:R_0201_0603Metric, symbol Device:R_US
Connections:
- net VDD_3V3 renamed VDD_3V6
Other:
- note removed: "GND tous gnd"
- note removed: "Max freq emmc pour ringing ?"
- note removed: "Ringing resistor (near mcu)"
- moved on the sheet: C29, D1, J1, J2, J3, J4, J5, J6, J7, R1, R10, R100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
